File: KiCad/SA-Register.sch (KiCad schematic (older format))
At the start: 42 parts, among them U10 74LVC1G32, U11 74LVC1G32, U12 74LVC1G32, U36 74HC74, U39 74HC74, U40 74HC74, U41 74HC74, U42 74LVC1G14, U5 74LVC1G32, U6 74LVC1G32, U7 74LVC1G32, U8 74LVC1G32, U9 74LVC1G32

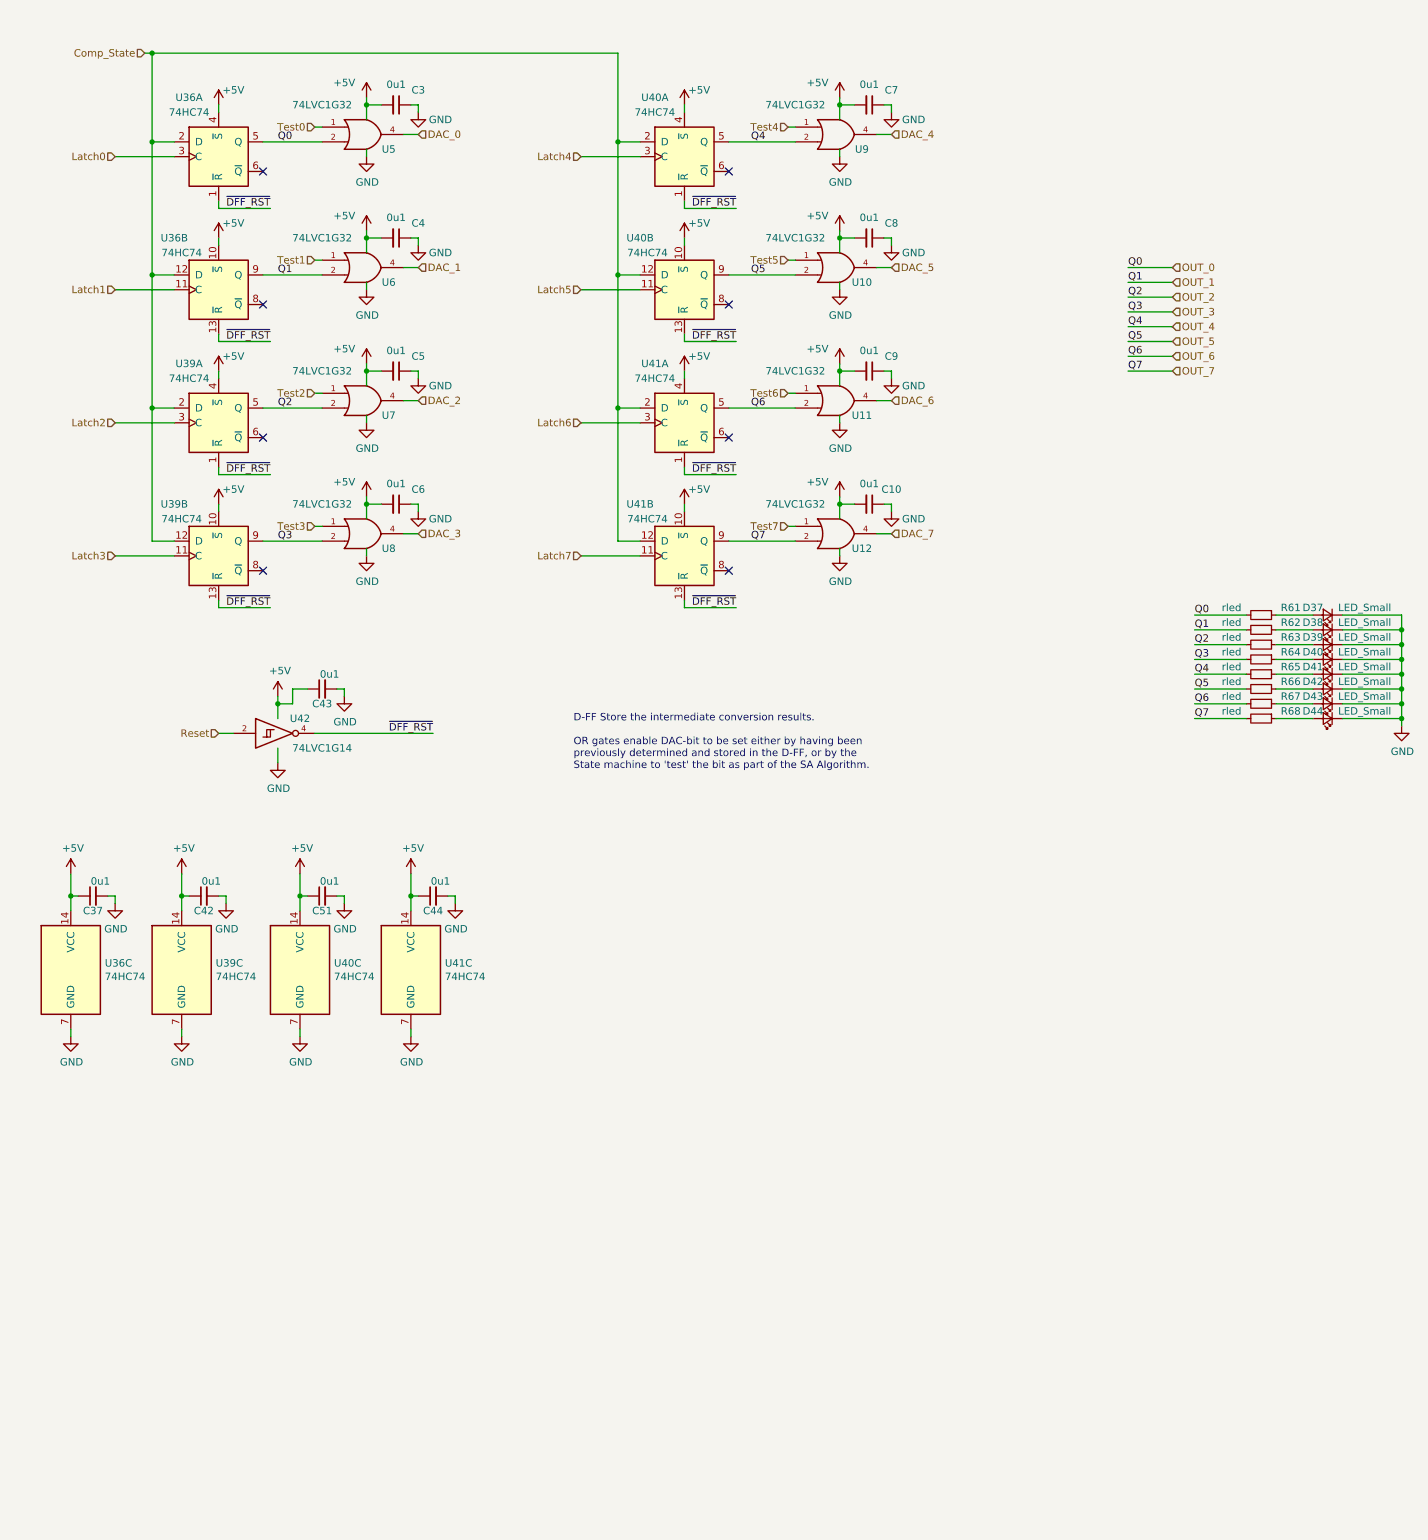
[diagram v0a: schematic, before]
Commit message: Schematic Update First Draft, ERC Passed
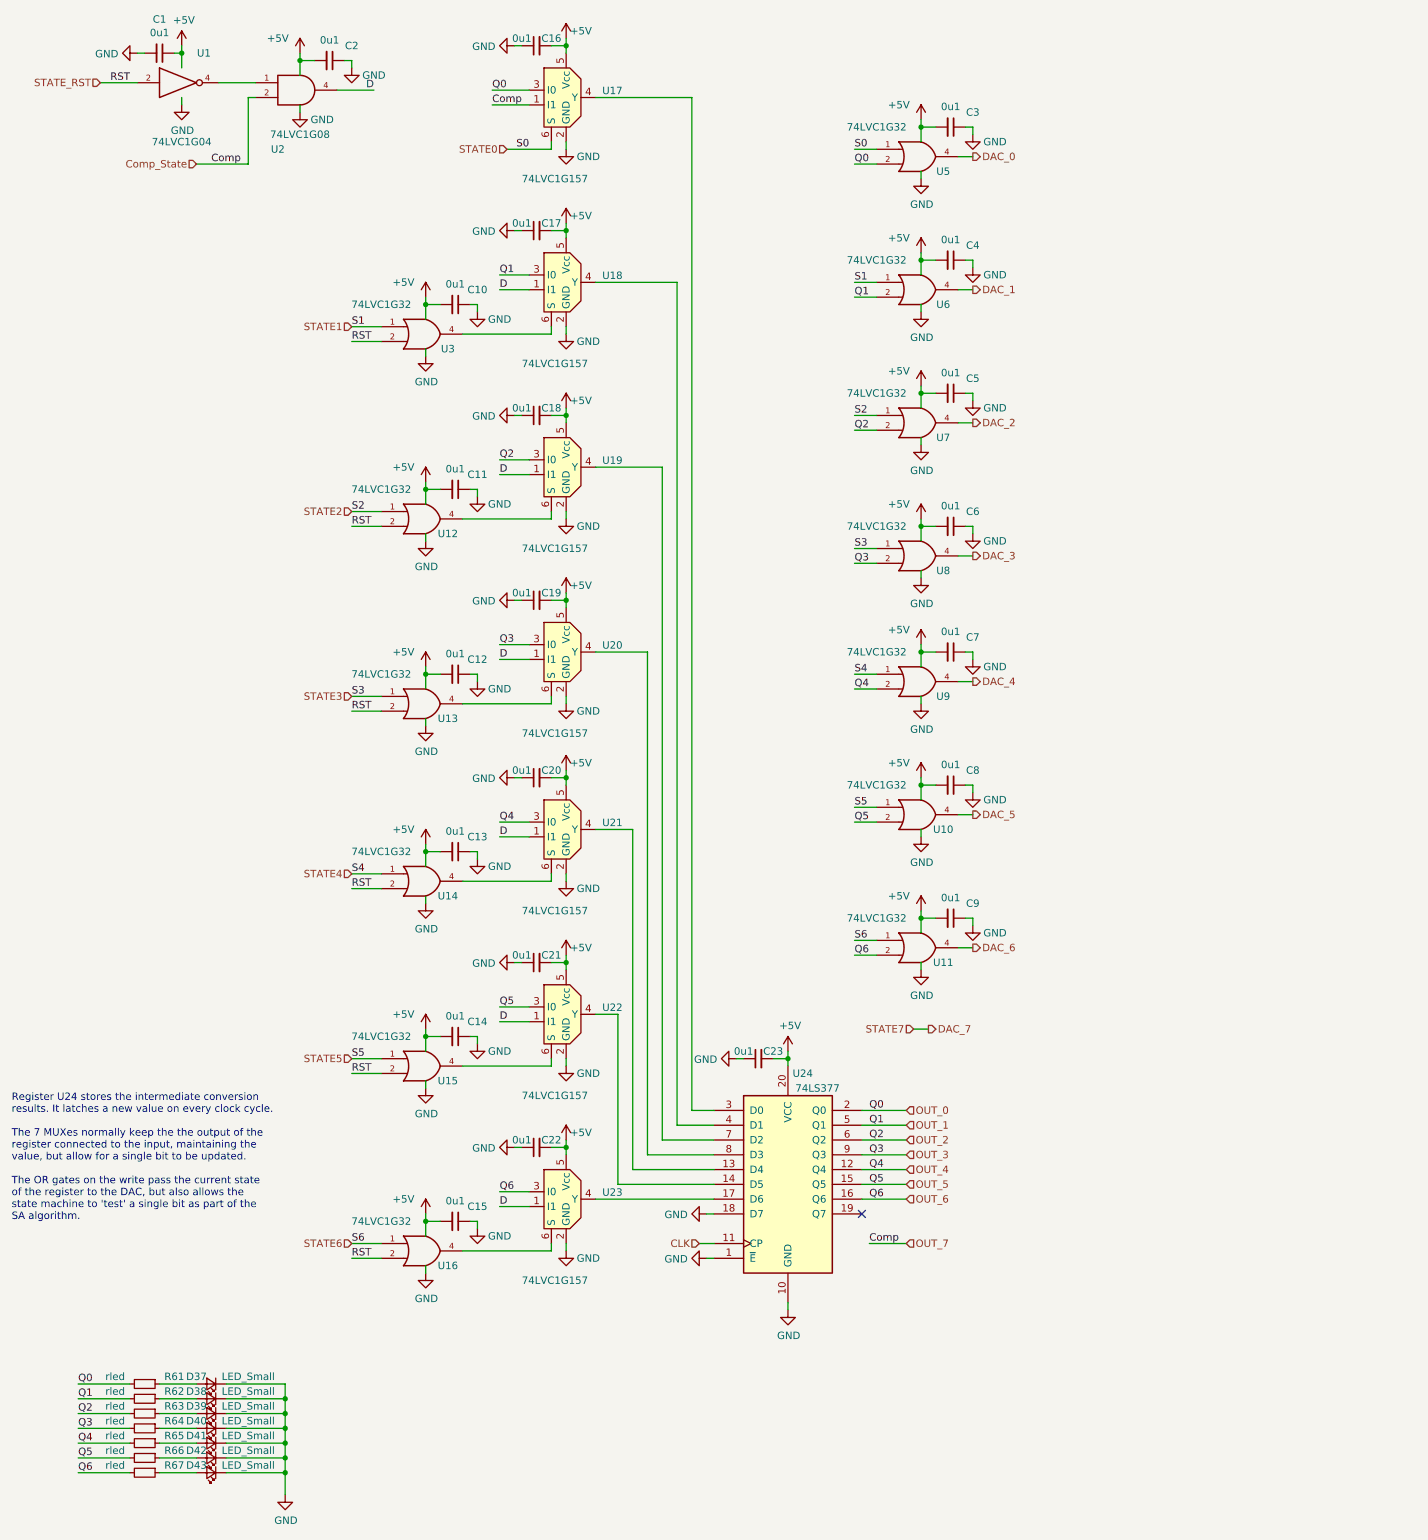
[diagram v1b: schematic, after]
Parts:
- removed C37, C42, C43, C44, C51: 0u1, Capacitor_SMD:C_0603_1608Metric, symbol Device:C_Small
- removed D44: LED_Small, LED_SMD:LED_0805_2012Metric, symbol Device:LED_Small
- removed R68: rled, Resistor_SMD:R_0603_1608Metric, symbol Device:R_Small
- removed U36, U39, U40, U41: 74HC74, Package_SO:TSSOP-14_4.4x5mm_P0.65mm, symbol 74xx:74HC74
- removed U42: 74LVC1G14, Package_TO_SOT_SMD:SOT-353_SC-70-5, symbol 74xGxx:74LVC1G14
- added C1, C11, C12, C13, C14, C15, C16, C17, C18, C19, C2, C20, C21, C22, C23: 0u1, Capacitor_SMD:C_0603_1608Metric, symbol Device:C_Small
- added U1: 74LVC1G04, Package_TO_SOT_SMD:SOT-353_SC-70-5, symbol 74xGxx:74LVC1G04
- added U13, U14, U15, U16, U3: 74LVC1G32, Package_TO_SOT_SMD:SOT-353_SC-70-5, symbol 74xGxx:74LVC1G32
- added U17, U18, U19, U20, U21, U22, U23: 74LVC1G157, Package_TO_SOT_SMD:SOT-363_SC-70-6, symbol 74LVC1G157:74LVC1G157
- added U2: 74LVC1G08, Package_TO_SOT_SMD:SOT-353_SC-70-5, symbol 74xGxx:74LVC1G08
- added U24: 74LS377, Package_SO:SOIC-20W_7.5x12.8mm_P1.27mm, symbol 74xx:74LS377
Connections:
- net Test7 is gone; now on net STATE2: U12.1
- net +5V: now also C1.1, C11.2, C12.2, C13.2, C14.2, C15.2, C16.2, C17.2, C18.2, C19.2, C2.2, C20.2, C21.2, C22.2, C23.2, U1.5 (VCC), U13.5 (VCC), U14.5 (VCC), U15.5 (VCC), U16.5 (VCC), U17.5 (Vcc), U18.5 (Vcc), U19.5 (Vcc), U2.5 (VCC), U20.5 (Vcc), U21.5 (Vcc), U22.5 (Vcc), U23.5 (Vcc), U24.20 (VCC), U3.5 (VCC)
- net Comp_State: now also U17.1 (I1), U2.2
- net DAC_7: no longer U12.4
- net GND: now also C1.2, C11.1, C12.1, C13.1, C14.1, C15.1, C16.1, C17.1, C18.1, C19.1, C2.1, C20.1, C21.1, C22.1, C23.1, U1.3 (GND), U13.3 (GND), U14.3 (GND), U15.3 (GND), U16.3 (GND), U17.2 (GND), U18.2 (GND), U19.2 (GND), U2.3 (GND), U20.2 (GND), U21.2 (GND), U22.2 (GND), U23.2 (GND), U24.1 (~E), U24.10 (GND), U24.18 (D7), U3.3 (GND)
- net OUT_0: now also U17.3 (I0), U24.2 (Q0)
- net OUT_1: now also U18.3 (I0), U24.5 (Q1)
- net OUT_2: now also U19.3 (I0), U24.6 (Q2)
- net OUT_3: now also U20.3 (I0), U24.9 (Q3)
- net OUT_4: now also U21.3 (I0), U24.12 (Q4)
- net OUT_5: now also U22.3 (I0), U24.15 (Q5)
- net OUT_6: now also U23.3 (I0), U24.16 (Q6)
- net OUT_7 renamed STATE_RST
- net STATE_RST: now also U1.2, U13.2, U14.2, U15.2, U16.2, U3.2
- net Test0 renamed STATE0
- net STATE0: now also U17.6 (S)
- net Test1 renamed STATE1
- net STATE1: now also U3.1
- net Test2 renamed STATE2
- net Test3 renamed STATE3
- net STATE3: now also U13.1
- net Test4 renamed STATE4
- net STATE4: now also U14.1
- net Test5 renamed STATE5
- net STATE5: now also U15.1
- net Test6 renamed STATE6
- net STATE6: now also U16.1
- new net: U21.4 (Y), U24.13 (D4)
- new net: U22.4 (Y), U24.14 (D5)
- new net: U23.4 (Y), U24.17 (D6)
- new net: U17.4 (Y), U24.3 (D0)
- new net: U18.4 (Y), U24.4 (D1)
- new net: U19.4 (Y), U24.7 (D2)
- new net: U20.4 (Y), U24.8 (D3)
- new net: U18.6 (S), U3.4
- new net: U12.4, U19.6 (S)
- new net: U13.4, U20.6 (S)
- new net: U14.4, U21.6 (S)
- new net: U15.4, U22.6 (S)
- new net: U16.4, U23.6 (S)
- new net: U1.4, U2.1
- new net CLK: U24.11 (CP)
- new net D: U18.1 (I1), U19.1 (I1), U2.4, U20.1 (I1), U21.1 (I1), U22.1 (I1), U23.1 (I1)
- no-connect marks 8 -> 1
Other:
- note added: "Register U24 stores the intermediate conversion\nresults. It latches a new value on every clock cycle.\n\nThe 7 MUXes normally keep the the output of the\nregister connected to the input, maintaining the \nvalue, but allow for a single bit to be updated.\n\nThe OR gates on the write pass the current state\nof the register to the DAC, but also allows the \nstate machine to 'test' a single bit as p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"
- note removed: "D-FF Store the intermediate conversion results.\n\nOR gates enable DAC-bit to be set either by having been \npreviously determined and stored in the D-FF, or by the \nState machine to 'test' the bit as part of the SA Algorithm."
- moved on the sheet: C3, C4, C5, C6, C7, C8, C9, D37, D38, D39, D40, D41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

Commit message: First part placement
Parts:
- D37, D38, D39, D40, D41, D42, D43: footprint LED_SMD:LED_0805_2012Metric -> LED_SMD:LED_0603_1608Metric
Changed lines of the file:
@@
 F 0 "D37" H 2000 9800 50  0000 C CNN
 F 1 "LED_Small" H 1650 9800 50  0000 C CNN
-F 2 "LED_SMD:LED_0805_2012Metric" V 1900 9850 50  0001 C CNN
+F 2 "LED_SMD:LED_0603_1608Metric" V 1900 9850 50  0001 C CNN
 F 3 "~" V 1900 9850 50  0001 C CNN
 	1    1900 9850
@@
 F 0 "D43" H 2000 10400 50  0000 C CNN
 F 1 "LED_Small" H 1650 10400 50  0000 C CNN
-F 2 "LED_SMD:LED_0805_2012Metric" V 1900 10450 50  0001 C CNN
+F 2 "LED_SMD:LED_0603_1608Metric" V 1900 10450 50  0001 C CNN
 F 3 "~" V 1900 10450 50  0001 C CNN
 	1    1900 10450
@@
 F 0 "D42" H 2000 10300 50  0000 C CNN
 F 1 "LED_Small" H 1650 10300 50  0000 C CNN
-F 2 "LED_SMD:LED_0805_2012Metric" V 1900 10350 50  0001 C CNN
+F 2 "LED_SMD:LED_0603_1608Metric" V 1900 10350 50  0001 C CNN
 F 3 "~" V 1900 10350 50  0001 C CNN
 	1    1900 10350
@@
 F 0 "D41" H 2000 10200 50  0000 C CNN
 F 1 "LED_Small" H 1650 10200 50  0000 C CNN
-F 2 "LED_SMD:LED_0805_2012Metric" V 1900 10250 50  0001 C CNN
+F 2 "LED_SMD:LED_0603_1608Metric" V 1900 10250 50  0001 C CNN
 F 3 "~" V 1900 10250 50  0001 C CNN
 	1    1900 10250
@@
 F 0 "D40" H 2000 10100 50  0000 C CNN
 F 1 "LED_Small" H 1650 10100 50  0000 C CNN
-F 2 "LED_SMD:LED_0805_2012Metric" V 1900 10150 50  0001 C CNN
+F 2 "LED_SMD:LED_0603_1608Metric" V 1900 10150 50  0001 C CNN
 F 3 "~" V 1900 10150 50  0001 C CNN
 	1    1900 10150
@@
 F 0 "D39" H 2000 10000 50  0000 C CNN
 F 1 "LED_Small" H 1650 10000 50  0000 C CNN
-F 2 "LED_SMD:LED_0805_2012Metric" V 1900 10050 50  0001 C CNN
+F 2 "LED_SMD:LED_0603_1608Metric" V 1900 10050 50  0001 C CNN
 F 3 "~" V 1900 10050 50  0001 C CNN
 	1    1900 10050
@@
 F 0 "D38" H 2000 9900 50  0000 C CNN
 F 1 "LED_Small" H 1650 9900 50  0000 C CNN
-F 2 "LED_SMD:LED_0805_2012Metric" V 1900 9950 50  0001 C CNN
+F 2 "LED_SMD:LED_0603_1608Metric" V 1900 9950 50  0001 C CNN
 F 3 "~" V 1900 9950 50  0001 C CNN
 	1    1900 9950
